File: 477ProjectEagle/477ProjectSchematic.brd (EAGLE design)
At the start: 101.6 x 127 mm, 81 parts, among them J1 POWER_JACK_BAT, J2 POWER_JACK_12VOUT, J3 RJ11-6PTH, Q1 AO4419, X1 22-23-2051, X10 MOTORS

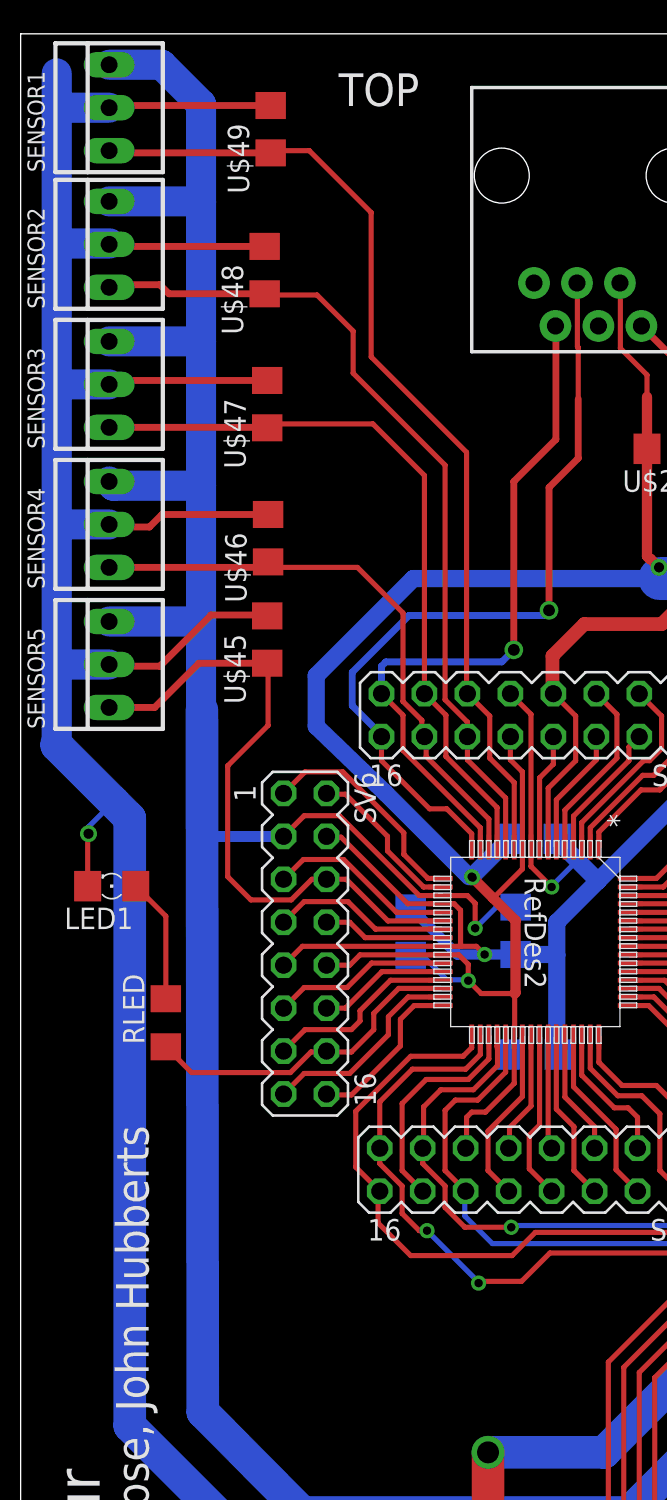
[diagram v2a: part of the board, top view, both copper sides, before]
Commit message: Scott lab - Minor tweaks to main PCB
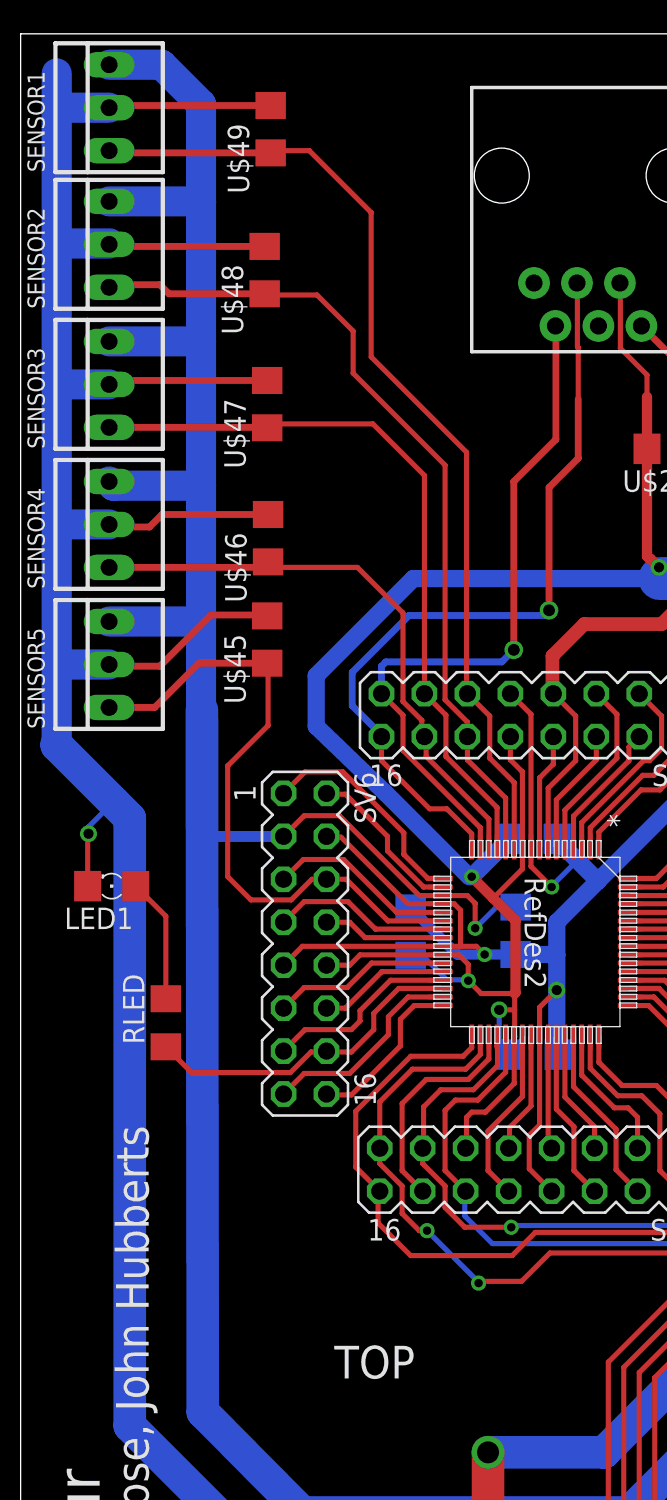
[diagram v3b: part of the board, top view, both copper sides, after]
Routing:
- net +3V3: track 250.2 -> 254.3 mm
- net GND: track 923.6 -> 926.8 mm
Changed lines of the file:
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@@
 <rectangle x1="74.4728" y1="103.1748" x2="75.5396" y2="103.6828" layer="1"/>
 <text x="2.1336" y="42.164" size="2.54" layer="21" rot="R270">Team 16: Project Minotaur</text>
-<text x="23.5712" y="124.6632" size="1.9304" layer="21" rot="R180">TOP</text>
+<text x="23.3172" y="49.4284" size="1.9304" layer="21" rot="R180">TOP</text>
 <text x="7.5692" y="2.6416" size="1.9304" layer="21" rot="R90">Scott Stack, Neil Kumar, Jon Roose, John Hubberts</text>
 </plain>
@@
 <param name="mtCopper" value="0.035mm 0.035mm 0.035mm 0.035mm 0.035mm 0.035mm 0.035mm 0.035mm 0.035mm 0.035mm 0.035mm 0.035mm 0.035mm 0.035mm 0.035mm 0.035mm"/>
 <param name="mtIsolate" value="1.5mm 0.15mm 0.2mm 0.15mm 0.2mm 0.15mm 0.2mm 0.15mm 0.2mm 0.15mm 0.2mm 0.15mm 0.2mm 0.15mm 0.2mm"/>
-<param name="mdWireWire" value="12mil"/>
-<param name="mdWirePad" value="12mil"/>
-<param name="mdWireVia" value="12mil"/>
+<param name="mdWireWire" value="8mil"/>
+<param name="mdWirePad" value="8mil"/>
+<param name="mdWireVia" value="8mil"/>
 <param name="mdPadPad" value="8mil"/>
 <param name="mdPadVia" value="8mil"/>
@@
 <wire x1="5.2324" y1="122.6312" x2="2.2352" y2="122.6312" width="1.778" layer="16"/>
 <wire x1="2.2352" y1="122.6312" x2="2.1336" y2="122.5296" width="1.778" layer="16"/>
-<via x="5.2832" y="114.6048" extent="1-16" drill="0.6" shape="square"/>
 <wire x1="5.2832" y1="114.6048" x2="2.4384" y2="114.6048" width="1.778" layer="16"/>
 <wire x1="2.4384" y1="114.6048" x2="2.1336" y2="114.9096" width="1.778" layer="16"/>
@@
 <wire x1="31.6992" y1="68.4784" x2="31.6992" y2="66.7288" width="0.8128" layer="16"/>
 <wire x1="31.6992" y1="66.7288" x2="31.7784" y2="66.6496" width="0.8128" layer="16"/>
-<wire x1="31.6992" y1="68.4784" x2="31.6992" y2="72.5424" width="1.016" layer="16"/>
+<wire x1="31.6992" y1="68.4784" x2="31.6992" y2="70.4596" width="1.016" layer="16"/>
+<wire x1="31.6992" y1="70.4596" x2="31.6992" y2="72.5424" width="1.016" layer="16"/>
 <wire x1="31.6992" y1="72.5424" x2="31.6992" y2="74.4728" width="1.016" layer="16"/>
 <wire x1="29.2608" y1="72.5648" x2="31.6768" y2="72.5648" width="1.016" layer="16"/>
@@
 <wire x1="61.5696" y1="111.6584" x2="61.5696" y2="92.3544" width="0.3048" layer="1"/>
 <wire x1="61.5696" y1="92.3544" x2="60.6044" y2="91.3892" width="0.3048" layer="1"/>
-<wire x1="31.6992" y1="68.4784" x2="30.6832" y2="67.691" width="0" layer="19" extent="1-16"/>
+<wire x1="30.6832" y1="67.691" x2="30.6832" y2="69.4436" width="0.3048" layer="1"/>
+<wire x1="30.6832" y1="69.4436" x2="31.6992" y2="70.4596" width="0.3048" layer="1"/>
+<via x="31.6992" y="70.4596" extent="1-16" drill="0.6"/>
+<wire x1="5.2832" y1="114.6048" x2="5.2324" y2="114.554" width="0.3048" layer="16"/>
 </signal>
 <signal name="N$16">
@@
 <wire x1="26.4668" y1="71.9836" x2="25.908" y2="72.5424" width="0.3048" layer="1"/>
 <wire x1="25.908" y1="72.5424" x2="24.8158" y2="72.5424" width="0.3048" layer="1"/>
-<via x="26.7208" y="77.1144" extent="1-16" drill="0.5"/>
 <wire x1="26.7208" y1="77.1144" x2="27.94" y2="75.8952" width="0.6096" layer="1"/>
 <wire x1="27.94" y1="75.8952" x2="29.2608" y2="74.5744" width="0.6096" layer="1"/>
 <wire x1="29.2608" y1="74.5744" x2="29.2608" y2="70.3072" width="0.6096" layer="1"/>
 <wire x1="29.2608" y1="70.3072" x2="29.21" y2="70.2564" width="0.6096" layer="1"/>
-<wire x1="29.21" y1="70.2564" x2="29.21" y2="67.7164" width="0.3048" layer="1"/>
+<wire x1="29.21" y1="70.2564" x2="29.21" y2="69.2912" width="0.3048" layer="1"/>
+<wire x1="29.21" y1="69.2912" x2="29.21" y2="67.7164" width="0.3048" layer="1"/>
 <wire x1="29.21" y1="67.7164" x2="29.1846" y2="67.691" width="0.3048" layer="1"/>
 <wire x1="29.21" y1="70.2564" x2="27.2288" y2="70.2564" width="0.3048" layer="1"/>
@@
 <wire x1="59.6392" y1="95.4024" x2="59.5884" y2="95.3516" width="0.3048" layer="16"/>
 <wire x1="59.5884" y1="95.3516" x2="59.5884" y2="94.7928" width="0.3048" layer="16"/>
-<wire x1="29.1846" y1="67.691" x2="28.9784" y2="66.6496" width="0" layer="19" extent="1-16"/>
+<wire x1="29.1846" y1="67.691" x2="29.21" y2="67.691" width="0.3048" layer="1"/>
+<wire x1="29.21" y1="67.691" x2="29.21" y2="67.7164" width="0.3048" layer="1"/>
+<wire x1="29.21" y1="69.2912" x2="28.2956" y2="69.2912" width="0.3048" layer="1"/>
+<via x="28.2956" y="69.2912" extent="1-16" drill="0.6"/>
+<wire x1="28.2956" y1="69.2912" x2="28.2956" y2="67.3324" width="0.3048" layer="16"/>
+<wire x1="28.2956" y1="67.3324" x2="28.9784" y2="66.6496" width="0.3048" layer="16"/>
+<wire x1="26.8478" y1="76.9874" x2="26.7208" y2="77.1144" width="0.3048" layer="16"/>
 </signal>
 <signal name="+12V">

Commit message: minor changes to PCBs
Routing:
- net +3V3: track 254.3 -> 255.2 mm
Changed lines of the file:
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@@
 <setting verticaltext="up"/>
 </settings>
-<grid distance="2" unitdist="mil" unit="mil" style="lines" multiple="1" display="yes" altdistance="0.025" altunitdist="inch" altunit="inch"/>
+<grid distance="8" unitdist="mil" unit="mil" style="lines" multiple="1" display="yes" altdistance="0.025" altunitdist="inch" altunit="inch"/>
 <layers>
 <layer number="1" name="Top" color="4" fill="1" visible="yes" active="yes"/>
@@
 <text x="23.3172" y="49.4284" size="1.9304" layer="21" rot="R180">TOP</text>
 <text x="7.5692" y="2.6416" size="1.9304" layer="21" rot="R90">Scott Stack, Neil Kumar, Jon Roose, John Hubberts</text>
+<rectangle x1="24.5872" y1="27.8384" x2="28.2448" y2="29.464" layer="1"/>
+<rectangle x1="24.7904" y1="13.6144" x2="28.0416" y2="15.4432" layer="1"/>
 </plain>
 <attributes>
@@
 <wire x1="17.4752" y1="89.0524" x2="17.4752" y2="86.0552" width="1.016" layer="16"/>
 <wire x1="17.4752" y1="86.0552" x2="21.5392" y2="82.1436" width="1.016" layer="16"/>
-<wire x1="21.5392" y1="82.1436" x2="26.5176" y2="77.1652" width="1.016" layer="16"/>
-<via x="26.67" y="77.1652" extent="1-16" drill="0.5"/>
+<wire x1="21.5392" y1="82.1436" x2="25.908" y2="77.7748" width="1.016" layer="16"/>
+<wire x1="25.908" y1="77.7748" x2="26.5176" y2="77.1652" width="1.016" layer="16"/>
 <wire x1="26.67" y1="77.1652" x2="26.5176" y2="77.1652" width="0.4064" layer="16"/>
 <wire x1="26.7208" y1="77.1144" x2="26.67" y2="77.1652" width="0.4064" layer="16"/>
@@
 <wire x1="26.4668" y1="71.9836" x2="25.908" y2="72.5424" width="0.3048" layer="1"/>
 <wire x1="25.908" y1="72.5424" x2="24.8158" y2="72.5424" width="0.3048" layer="1"/>
-<wire x1="26.7208" y1="77.1144" x2="27.94" y2="75.8952" width="0.6096" layer="1"/>
 <wire x1="27.94" y1="75.8952" x2="29.2608" y2="74.5744" width="0.6096" layer="1"/>
 <wire x1="29.2608" y1="74.5744" x2="29.2608" y2="70.3072" width="0.6096" layer="1"/>
@@
 <wire x1="28.2956" y1="69.2912" x2="28.2956" y2="67.3324" width="0.3048" layer="16"/>
 <wire x1="28.2956" y1="67.3324" x2="28.9784" y2="66.6496" width="0.3048" layer="16"/>
-<wire x1="26.8478" y1="76.9874" x2="26.7208" y2="77.1144" width="0.3048" layer="16"/>
+<wire x1="27.94" y1="75.8952" x2="26.7208" y2="77.1144" width="0.6096" layer="1"/>
+<via x="26.7208" y="77.1144" extent="1-16" drill="0.8"/>
+<wire x1="26.7208" y1="77.1144" x2="26.5684" y2="77.1144" width="0.6096" layer="16"/>
+<wire x1="26.5684" y1="77.1144" x2="25.908" y2="77.7748" width="0.6096" layer="16"/>
 </signal>
 <signal name="+12V">

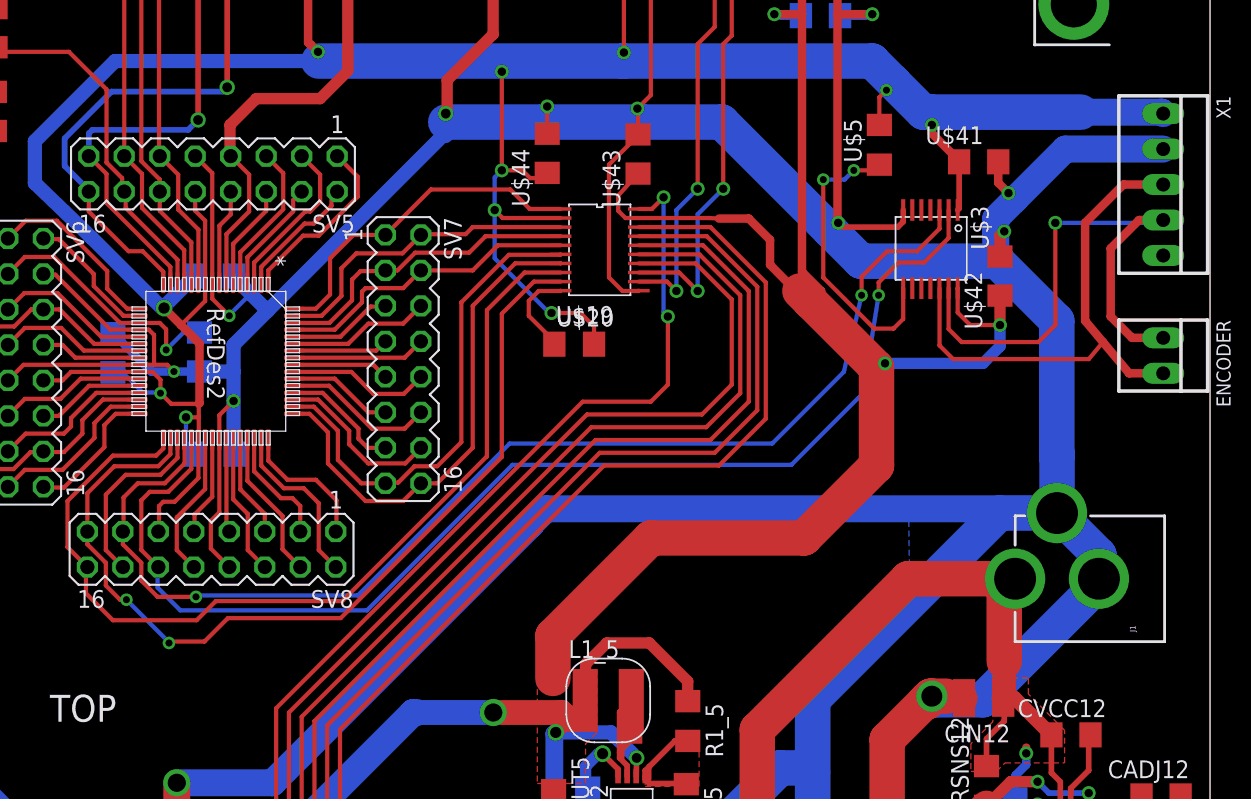
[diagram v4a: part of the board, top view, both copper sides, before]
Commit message: Changes to main PCB!!!
Took out I2C level converter. Changed encoder to GPIO pins
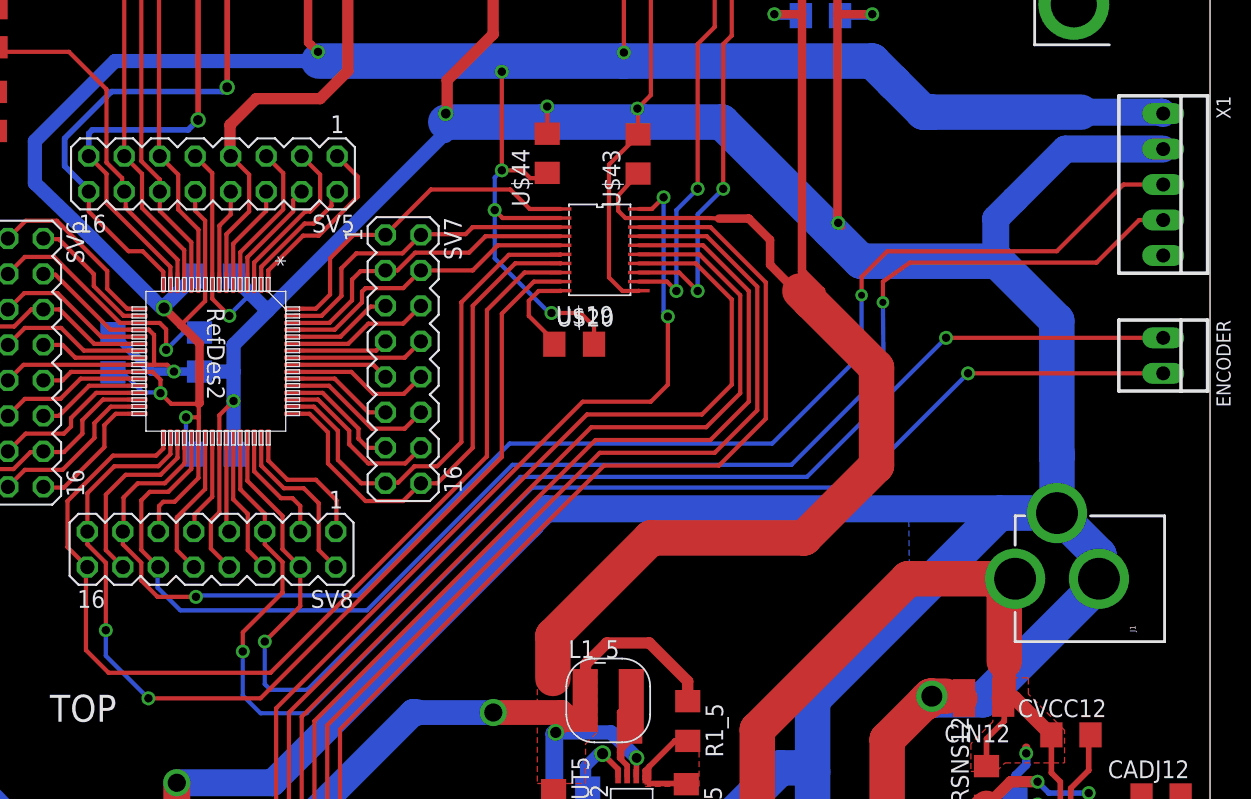
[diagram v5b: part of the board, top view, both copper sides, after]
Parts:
- removed U$3: TXS0104E, MinotaurParts:SSOP-14
- removed U$41, U$42: 10uF, MinotaurParts:C1206
- removed U$5: 10k, MinotaurParts:R1206
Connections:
- removed net N$12: SV8.12, U$1.37, U$3.2
- removed net N$13: SV8.13, U$1.36, U$3.3
- removed net N$92: U$3.8, U$5.1
- net +3V3: no longer U$3.1, U$41.1, U$5.2
- net +5V: no longer U$3.14, U$42.1
- net GND: no longer U$3.7, U$41.2, U$42.2
- net N$70: now also ENCODER.1
- net N$71: now also ENCODER.2
- net SCL: now also SV8.12, U$1.37; no longer ENCODER.1, U$3.13
- net SDA: now also SV8.13, U$1.36; no longer ENCODER.2, U$3.12
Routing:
- net N$71: track 7.30 -> 97.2 mm, vias 0 -> 2
- net N$12: track 87.3 -> 0.00 mm, vias 1 -> 0
- net N$13: track 86.3 -> 0.00 mm, vias 2 -> 0
- net N$70: track 10.7 -> 95.0 mm, vias 0 -> 2
- net SDA: track 37.9 -> 102.7 mm, vias 0 -> 2
- net SCL: track 40.4 -> 101.3 mm
- net N$92: track 21.2 -> 0.00 mm, vias 2 -> 0
- net +5V: track 333.5 -> 316.0 mm, vias 7 -> 5
- net GND: track 926.8 -> 916.4 mm, vias 21 -> 19
- net +3V3: track 255.2 -> 245.5 mm, vias 11 -> 9
- net N$8: track 66.3 -> 72.5 mm
- net N$9: track 67.5 -> 73.0 mm

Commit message: Fixed thermals and traces on RJ-11 connector
Scott Lab
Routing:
- net N$7: track 47.2 -> 59.8 mm, vias 1 -> 2
- net +3V3: track 245.5 -> 250.4 mm, vias 9 -> 10
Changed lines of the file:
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@@
 <setting verticaltext="up"/>
 </settings>
-<grid distance="2" unitdist="mil" unit="mil" style="lines" multiple="1" display="yes" altdistance="0.025" altunitdist="inch" altunit="inch"/>
+<grid distance="8" unitdist="mil" unit="mil" style="lines" multiple="1" display="yes" altdistance="0.025" altunitdist="inch" altunit="inch"/>
 <layers>
 <layer number="1" name="Top" color="4" fill="1" visible="yes" active="yes"/>
@@
 <text x="23.3172" y="49.4284" size="1.9304" layer="21" rot="R180">TOP</text>
 <text x="7.5692" y="2.6416" size="1.9304" layer="21" rot="R90">Scott Stack, Neil Kumar, Jon Roose, John Hubberts</text>
-<rectangle x1="24.5872" y1="27.8384" x2="28.2448" y2="29.464" layer="1"/>
-<rectangle x1="24.7904" y1="13.6144" x2="28.0416" y2="15.4432" layer="1"/>
 </plain>
 <attributes>
@@
 <wire x1="87.9634" y1="15.4178" x2="87.9634" y2="11.7006" width="2.54" layer="1"/>
 <wire x1="87.9634" y1="11.7006" x2="90.011" y2="9.653" width="2.54" layer="1"/>
-<polygon width="0.3048" layer="1">
+<polygon width="0.3048" layer="1" thermals="no">
 <vertex x="53.848" y="40.2336"/>
 <vertex x="53.848" y="36.3728"/>
@@
 <vertex x="32.7152" y="27.0256"/>
 <vertex x="32.7152" y="28.0416"/>
+<vertex x="28.0416" y="28.2448"/>
+<vertex x="28.0416" y="29.6672"/>
+<vertex x="24.7904" y="29.6672"/>
+<vertex x="24.7904" y="28.0416"/>
 <vertex x="20.1168" y="28.0416"/>
 <vertex x="20.066" y="25.654"/>
@@
 <vertex x="18.9992" y="14.5796"/>
 <vertex x="21.9456" y="14.5288"/>
+<vertex x="24.9936" y="14.4272"/>
+<vertex x="24.9936" y="13.4112"/>
+<vertex x="25.1968" y="13.4112"/>
+<vertex x="28.0416" y="13.4112"/>
+<vertex x="28.0416" y="14.4272"/>
 <vertex x="28.8036" y="14.4272"/>
 <vertex x="32.7152" y="14.478"/>
@@
 <contactref element="J3" pad="2"/>
 <wire x1="37.0336" y1="105.5366" x2="37.0336" y2="106.832" width="0.3048" layer="1"/>
-<wire x1="37.0336" y1="106.832" x2="35.4584" y2="108.4072" width="0.3048" layer="1"/>
-<wire x1="35.4584" y1="108.4072" x2="35.4584" y2="112.2426" width="0.3048" layer="1"/>
-<wire x1="35.4584" y1="112.2426" x2="35.433" y2="112.268" width="0.3048" layer="1"/>
 <contactref element="RLED2" pad="1"/>
 <wire x1="63.0432" y1="117.5512" x2="59.6392" y2="114.1472" width="0.3048" layer="1"/>
@@
 <wire x1="26.7208" y1="77.1144" x2="26.5684" y2="77.1144" width="0.6096" layer="16"/>
 <wire x1="26.5684" y1="77.1144" x2="25.908" y2="77.7748" width="0.6096" layer="16"/>
+<via x="37.0336" y="106.832" extent="1-16" drill="0.6"/>
+<wire x1="37.0336" y1="106.832" x2="38.3536" y2="106.832" width="0.4064" layer="16"/>
+<wire x1="38.3536" y1="106.832" x2="40.2336" y2="108.712" width="0.4064" layer="16"/>
+<wire x1="40.2336" y1="108.712" x2="40.2336" y2="110.1344" width="0.4064" layer="16"/>
+<wire x1="40.2336" y1="110.1344" x2="38.2016" y2="112.1664" width="0.4064" layer="16"/>
+<wire x1="38.2016" y1="112.1664" x2="35.5346" y2="112.1664" width="0.4064" layer="16"/>
+<wire x1="35.5346" y1="112.1664" x2="35.433" y2="112.268" width="0.4064" layer="16"/>
 </signal>
 <signal name="+12V">
@@
 <wire x1="31.242" y1="100.1776" x2="32.9692" y2="101.9048" width="0.4064" layer="1"/>
 <contactref element="J3" pad="4"/>
-<wire x1="32.9692" y1="112.1918" x2="32.893" y2="112.268" width="0.3048" layer="1"/>
 <wire x1="32.9692" y1="101.9048" x2="32.9692" y2="105.41" width="0.4064" layer="1"/>
-<wire x1="32.9692" y1="105.41" x2="32.9692" y2="108.458" width="0.3048" layer="1"/>
-<wire x1="32.9692" y1="108.458" x2="32.9184" y2="108.5088" width="0.3048" layer="1"/>
-<wire x1="32.9184" y1="108.5088" x2="32.9184" y2="112.2426" width="0.3048" layer="1"/>
-<wire x1="32.9184" y1="112.2426" x2="32.893" y2="112.268" width="0.3048" layer="1"/>
+<via x="32.9692" y="105.41" extent="1-16" drill="0.6" shape="square"/>
+<wire x1="32.9692" y1="105.41" x2="30.1244" y2="105.41" width="0.4064" layer="16"/>
+<wire x1="30.1244" y1="105.41" x2="27.2288" y2="108.3056" width="0.4064" layer="16"/>
+<wire x1="27.2288" y1="108.3056" x2="27.2288" y2="112.776" width="0.4064" layer="16"/>
+<wire x1="27.2288" y1="112.776" x2="29.0576" y2="114.6048" width="0.4064" layer="16"/>
+<wire x1="29.0576" y1="114.6048" x2="31.9024" y2="114.6048" width="0.4064" layer="16"/>
+<wire x1="31.9024" y1="114.6048" x2="32.9184" y2="113.5888" width="0.4064" layer="16"/>
+<wire x1="32.9184" y1="113.5888" x2="32.9184" y2="112.2934" width="0.4064" layer="16"/>
+<wire x1="32.9184" y1="112.2934" x2="32.893" y2="112.268" width="0.4064" layer="16"/>
 </signal>
 <signal name="V+">
